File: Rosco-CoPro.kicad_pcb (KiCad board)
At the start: 4 copper layers, 53.2 x 89.9 mm, 16 parts, among them IC1 MC68882FN40A, IC2 ATF22V10, J1 Conn_01x03, X1 CXO_DIP8_40M

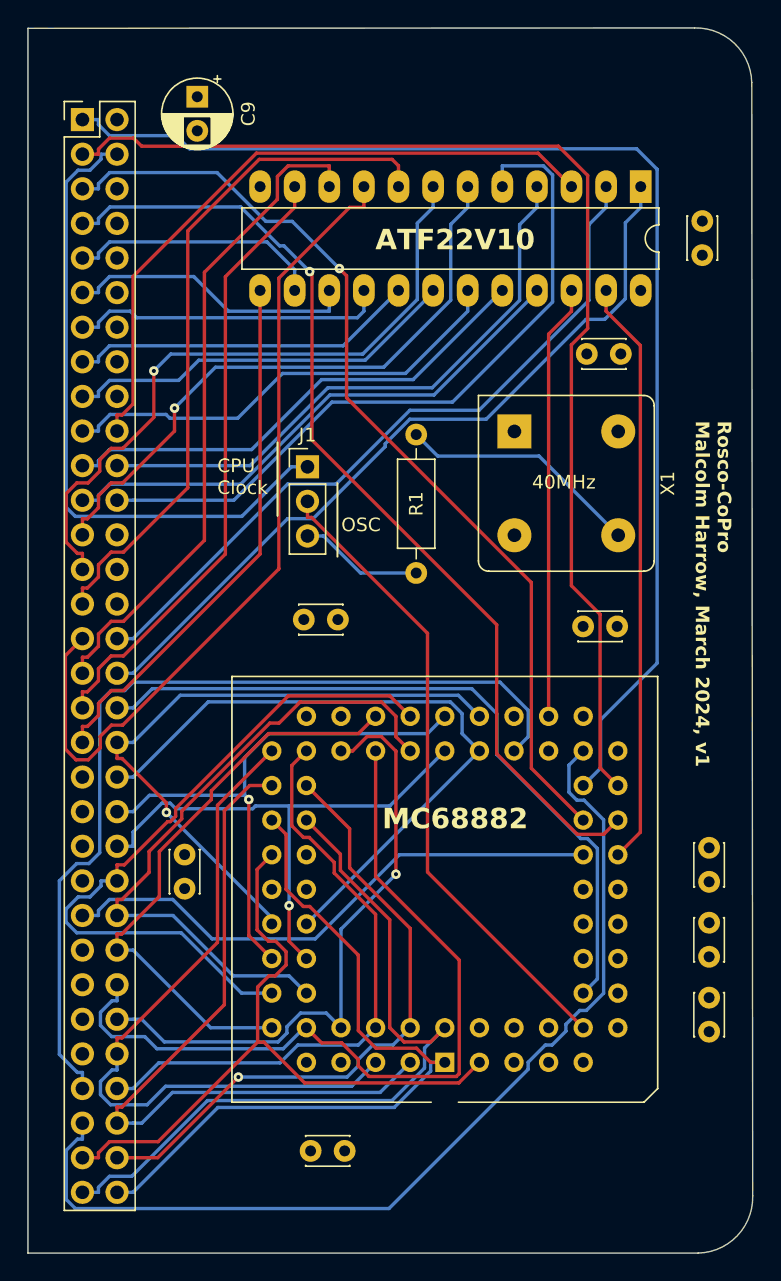
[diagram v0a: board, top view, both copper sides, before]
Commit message: v2 board plus improvements to test suite
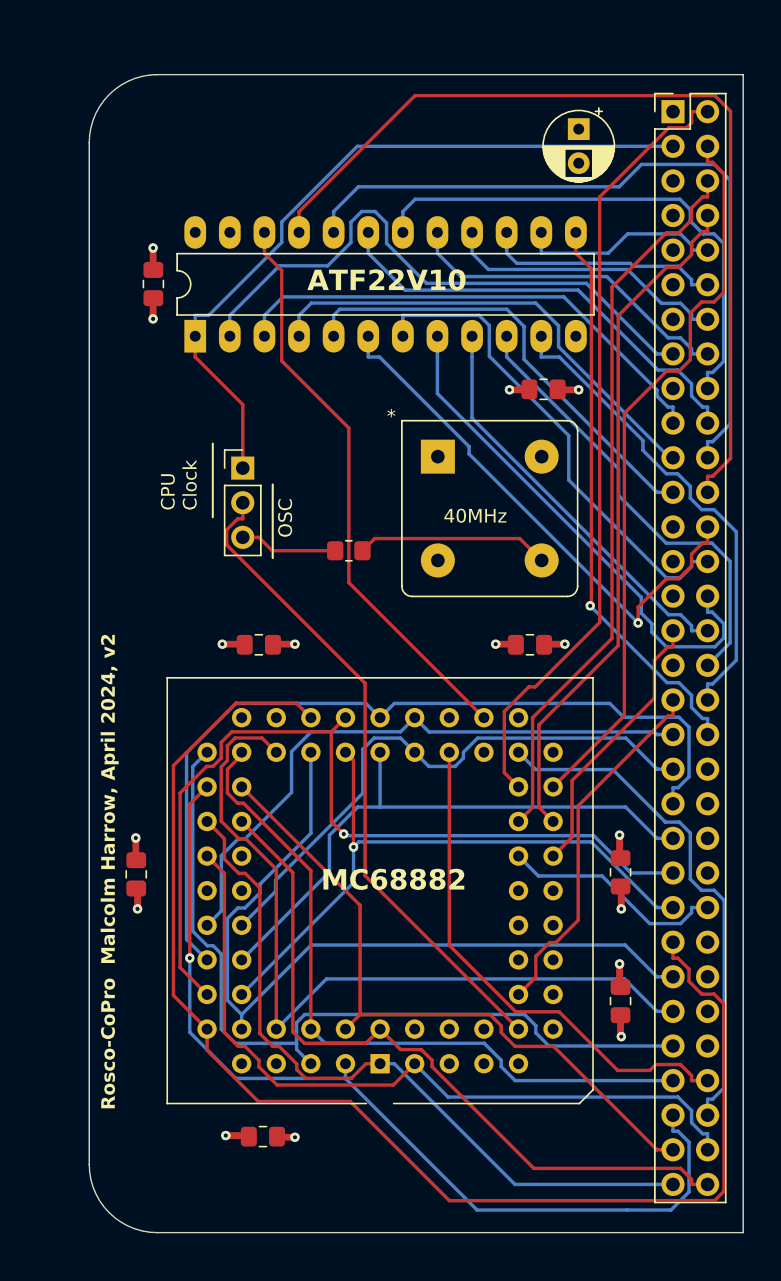
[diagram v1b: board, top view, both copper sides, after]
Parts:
- removed C8: 100nF, Capacitor_THT:C_Disc_D3.0mm_W2.0mm_P2.50mm
- C1, C10, C2, C3, C4, C5, C6, C7: footprint Capacitor_THT:C_Disc_D3.0mm_W2.0mm_P2.50mm -> Capacitor_SMD:C_0805_2012Metric_Pad1.18x1.45mm_HandSolder
- R1: footprint Resistor_THT:R_Axial_DIN0207_L6.3mm_D2.5mm_P10.16mm_Horizontal -> Resistor_SMD:R_0805_2012Metric_Pad1.20x1.40mm_HandSolder
- moved BUS1 43.4 mm to (81.8, 59.7)
- moved C10 40.3 mm to (43.7, 72.4), turned to -90 degrees
- moved IC2 34.5 mm to (46.8, 76.2), turned to 90 degrees
- moved C9 28.1 mm to (74.9, 61.0)
- moved R1 9.86 mm to (58.1, 91.9), turned to 180 degrees
- moved C4 6.88 mm to (78.0, 125.0)
- moved C7 6.54 mm to (78.0, 115.5)
- moved C1 6.24 mm to (72.3, 80.1)
- moved X1 5.92 mm to (64.6, 85.0)
- moved J1 4.75 mm to (50.3, 85.9)
- moved IC1 4.75 mm to (60.4, 129.6)
- moved C2 4.13 mm to (71.3, 98.8)
- moved C3 3.78 mm to (51.5, 98.8)
- moved C6 3.70 mm to (42.5, 115.7)
- moved C5 3.65 mm to (51.8, 134.9)
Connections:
- BUS1 pad 1: A1 -> +5V
- BUS1 pad 10: E -> A5
- BUS1 pad 11: A6 -> VMA
- BUS1 pad 12: VMA -> A6
- BUS1 pad 13: A7 -> MFPIEO
- BUS1 pad 14: MFPIEO -> A7
- BUS1 pad 15: A8 -> IOSEL
- BUS1 pad 16: IOSEL -> A8
- BUS1 pad 17: A9 -> EXPSEL
- BUS1 pad 18: EXPSEL -> A9
- BUS1 pad 19: A10 -> CPUFC0
- BUS1 pad 2: +5V -> A1
- BUS1 pad 20: CPUFC0 -> A10
- BUS1 pad 21: A11 -> CPUFC1
- BUS1 pad 22: CPUFC1 -> A11
- BUS1 pad 23: A12 -> CPUFC2
- BUS1 pad 24: CPUFC2 -> A12
- BUS1 pad 25: A13 -> IPL0
- BUS1 pad 26: IPL0 -> A13
- BUS1 pad 27: A14 -> IPL1
- BUS1 pad 28: IPL1 -> A14
- BUS1 pad 29: A15 -> IPL2
- BUS1 pad 3: A2 -> CPUCLK
- BUS1 pad 30: IPL2 -> A15
- BUS1 pad 31: A16 -> LDS
- BUS1 pad 32: LDS -> A16
- BUS1 pad 33: A17 -> UDS
- BUS1 pad 34: UDS -> A17
- BUS1 pad 35: A18 -> RESET
- BUS1 pad 36: RESET -> A18
- BUS1 pad 37: A19 -> D15
- BUS1 pad 38: D15 -> A19
- BUS1 pad 39: A20 -> D14
- BUS1 pad 4: CPUCLK -> A2
- BUS1 pad 40: D14 -> A20
- BUS1 pad 41: A21 -> D13
- BUS1 pad 42: D13 -> A21
- BUS1 pad 43: A22 -> D12
- BUS1 pad 44: D12 -> A22
- BUS1 pad 45: A23 -> D11
- BUS1 pad 46: D11 -> A23
- BUS1 pad 47: AS -> D10
- BUS1 pad 48: D10 -> AS
- BUS1 pad 49: BERR -> D9
- BUS1 pad 5: A3 -> GND
- BUS1 pad 50: D9 -> BERR
- BUS1 pad 51: BG -> D8
- BUS1 pad 52: D8 -> BG
- BUS1 pad 53: BGACK -> D7
- BUS1 pad 54: D7 -> BGACK
- BUS1 pad 55: BR -> D6
- BUS1 pad 56: D6 -> BR
- BUS1 pad 57: DTACK -> D5
- BUS1 pad 58: D5 -> DTACK
- BUS1 pad 59: RW -> D4
- BUS1 pad 6: GND -> A3
- BUS1 pad 60: D4 -> RW
- BUS1 pad 61: D0 -> D3
- BUS1 pad 62: D3 -> D0
- BUS1 pad 63: D1 -> D2
- BUS1 pad 64: D2 -> D1
- BUS1 pad 7: A4 -> VPA
- BUS1 pad 8: VPA -> A4
- BUS1 pad 9: A5 -> E
- IC1 pad 20: DS -> LDS
- IC2 pad 1: UDS -> CPUCLK
- IC2 pad 2: LDS -> IOSEL
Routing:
- net UDS: track 57.5 -> 0.00 mm
- net D9: track 42.8 -> 97.7 mm
- net IOSEL: track 0.00 -> 43.3 mm
- net DS: track 43.1 -> 0.00 mm
- net RW: track 72.8 -> 38.1 mm
- net A1: track 91.4 -> 57.9 mm
- net LDS: track 53.8 -> 20.4 mm
- net A16: track 62.2 -> 30.0 mm
- net A2: track 85.6 -> 54.0 mm
- net DTACK: track 67.4 -> 37.8 mm
- net RESET: track 53.5 -> 26.8 mm
- net A12: track 40.0 -> 66.1 mm
- net AS: track 41.2 -> 16.6 mm
- net A4: track 72.2 -> 50.8 mm, vias 1 -> 0
- net D13: track 41.4 -> 62.1 mm, vias 1 -> 0
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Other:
- board size 53.2 x 89.9 mm -> 48 x 85 mm
- board text added: "*"
- board text added: "Rosco-CoPro Malcolm Harrow, April 2024, v2"
- board text removed: "Rosco-CoPro Malcolm Harrow, March 2024, v1"
